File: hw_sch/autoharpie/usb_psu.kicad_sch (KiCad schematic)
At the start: 3 parts, among them J1 USB_C_Receptacle_USB2.0

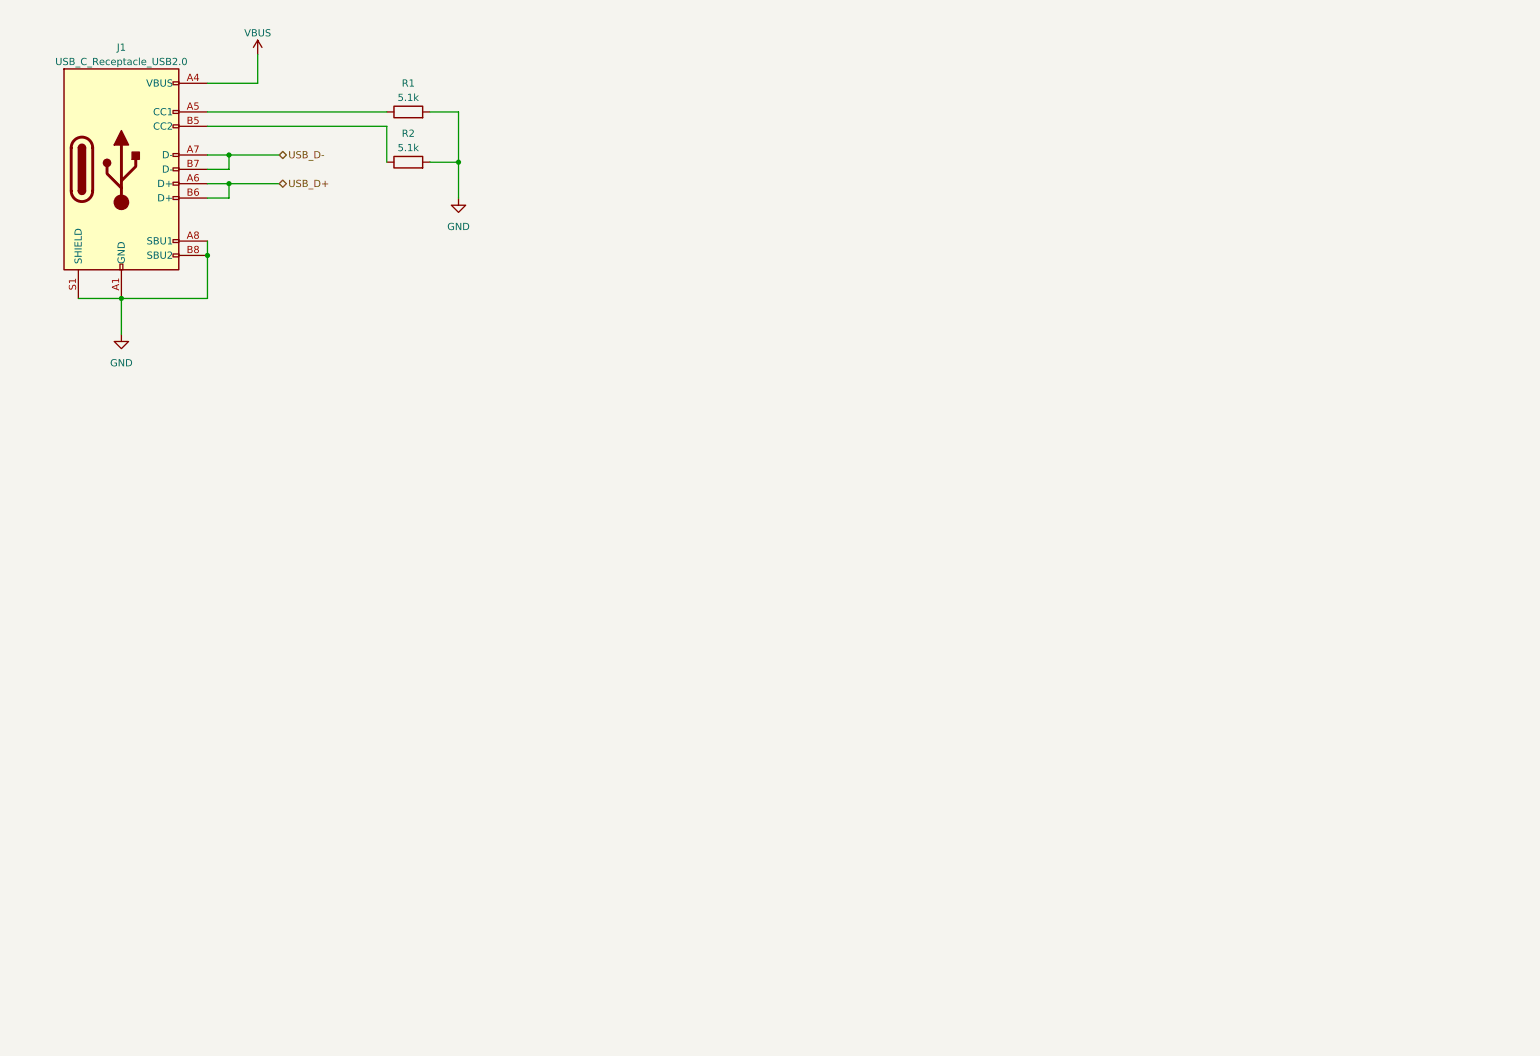
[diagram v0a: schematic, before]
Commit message: teensy mcu chip (imxrt), PSU subsystem work start
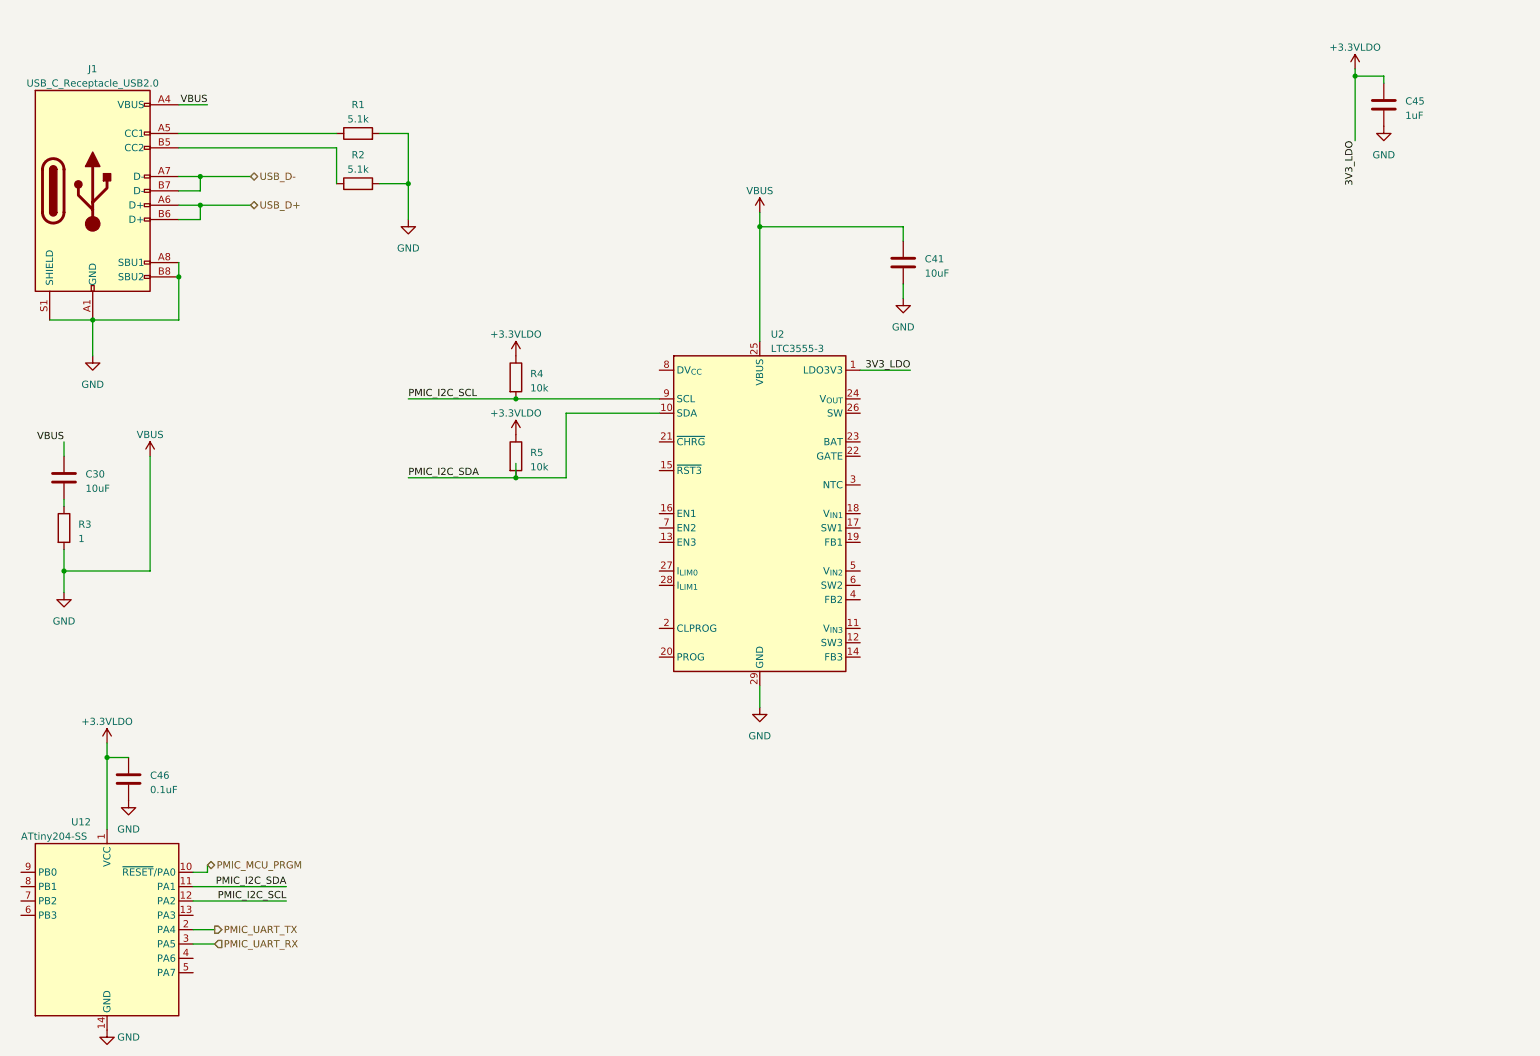
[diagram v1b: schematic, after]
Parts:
- added C30, C41: 10uF, symbol Device:C
- added C45: 1uF, symbol Device:C
- added C46: 0.1uF, symbol Device:C
- added R3: 1, symbol Device:R
- added R4, R5: 10k, symbol Device:R
- added U12: ATtiny204-SS, Package_SO:SOIC-8_3.9x4.9mm_P1.27mm, symbol MCU_Microchip_ATtiny:ATtiny204-SS
- added U2: LTC3555-3, Package_DFN_QFN:QFN-28-1EP_4x5mm_P0.5mm_EP2.65x3.65mm, symbol Battery_Management:LTC3555-3
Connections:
- net VBUS is gone; now on net GND: J1.A4 (VBUS), J1.A9 (VBUS), J1.B4 (VBUS), J1.B9 (VBUS)
- net GND: now also C30.1, C41.1, C41.2, C45.2, C46.2, R3.2, U12.14 (GND), U2.25 (VBUS), U2.29 (GND)
- new net: C30.2, R3.1
- new net +3.3V: C45.1, C46.1, R4.1, R5.1, U12.1 (VCC), U2.1 (LDO3V3)
- new net PMIC_I2C_SCL: R4.2, U12.12 (PA2), U2.9 (SCL)
- new net PMIC_I2C_SDA: R5.2, U12.11 (PA1), U2.10 (SDA)
- new net PMIC_MCU_PRGM: U12.10 (~{RESET}/PA0)
- new net PMIC_UART_RX: U12.3 (PA5)
- new net PMIC_UART_TX: U12.2 (PA4)
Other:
- moved on the sheet: J1, R1, R2

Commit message: switch to teensy reduce pins
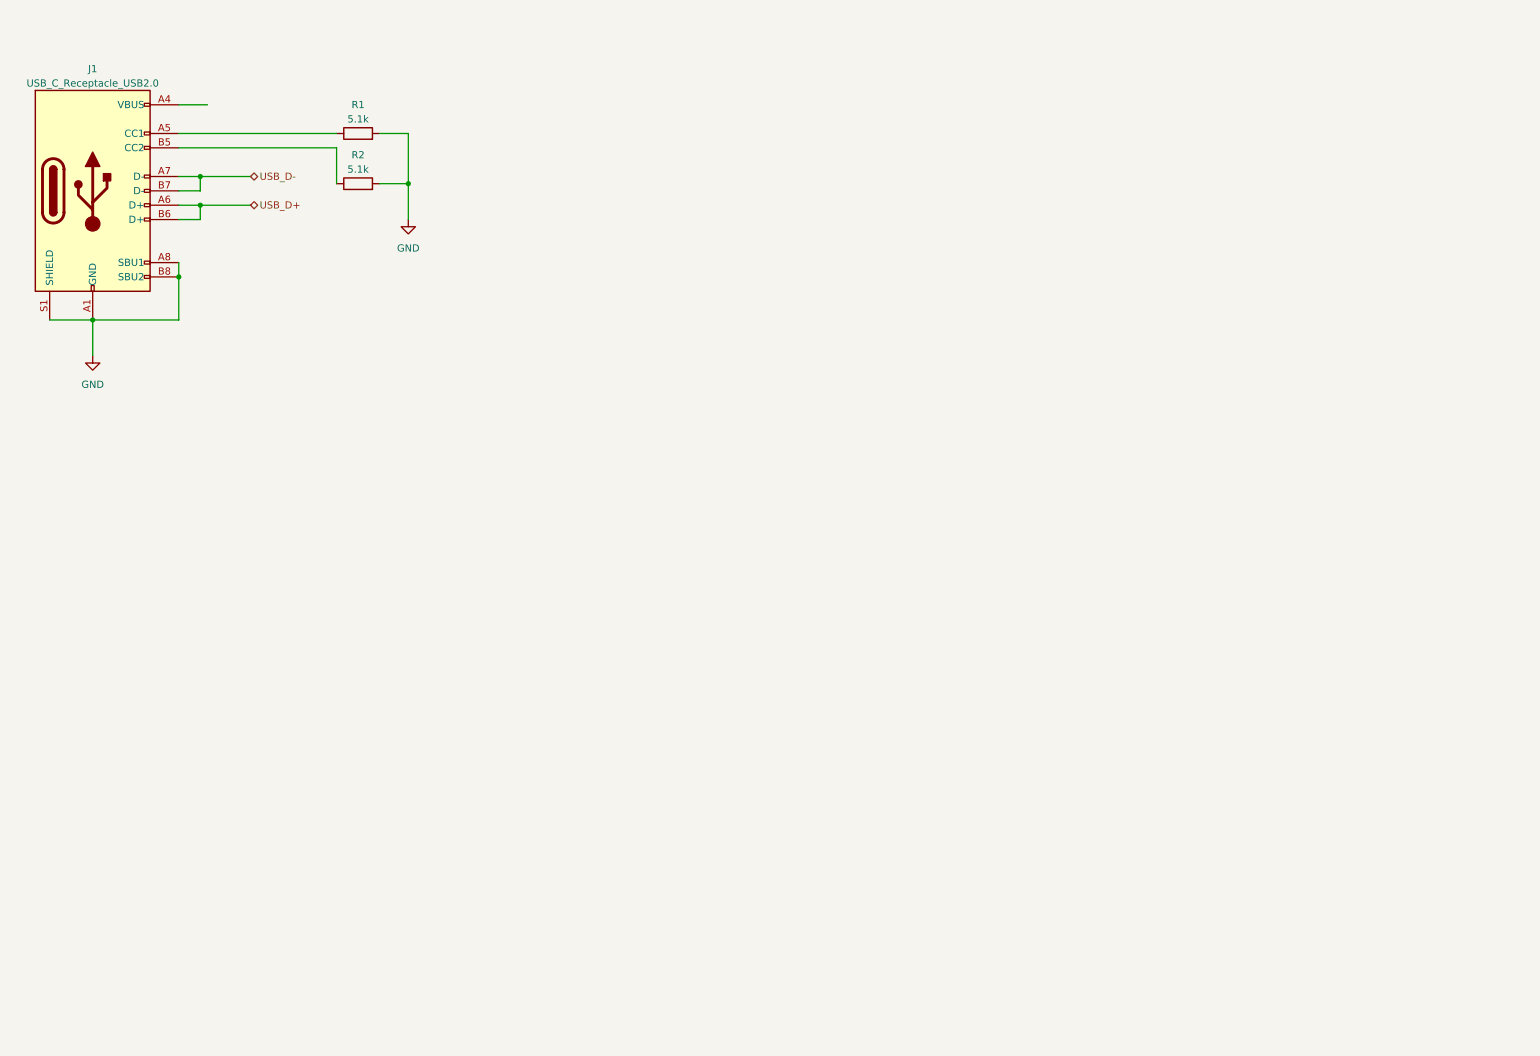
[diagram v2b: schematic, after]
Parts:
- removed C30, C41: 10uF, symbol Device:C
- removed C45: 1uF, symbol Device:C
- removed C46: 0.1uF, symbol Device:C
- removed R3: 1, symbol Device:R
- removed R4, R5: 10k, symbol Device:R
- removed U12: ATtiny204-SS, Package_SO:SOIC-8_3.9x4.9mm_P1.27mm, symbol MCU_Microchip_ATtiny:ATtiny204-SS
- removed U2: LTC3555-3, Package_DFN_QFN:QFN-28-1EP_4x5mm_P0.5mm_EP2.65x3.65mm, symbol Battery_Management:LTC3555-3
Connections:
- net GND: no longer J1.A4 (VBUS), J1.A9 (VBUS), J1.B4 (VBUS), J1.B9 (VBUS)
- new net: J1.A4 (VBUS), J1.A9 (VBUS), J1.B4 (VBUS), J1.B9 (VBUS)

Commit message: matrix, flattening
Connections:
- net VBUS: now reaches J1.A4 (VBUS), J1.A9 (VBUS), J1.B4 (VBUS), J1.B9 (VBUS)
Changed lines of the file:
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@@
   (junction (at 86.36 44.45) (diameter 0) (color 0 0 0 0)
   )
+  (wire (pts (xy 49.53 27.94) (xy 49.53 30.48))
+    (stroke (width 0) (type default))
+  )
   (wire (pts (xy 86.36 35.56) (xy 86.36 44.45))
     (stroke (width 0) (type default))
@@
     (stroke (width 0) (type default))
   )
-  (wire (pts (xy 45.72 30.48) (xy 50.8 30.48))
+  (wire (pts (xy 45.72 30.48) (xy 49.53 30.48))
     (stroke (width 0) (type default))
   )
@@
         )
       )
+    )
+  )
+  (symbol (lib_id "power:VBUS") (at 49.53 27.94 0) (unit 1)
+    (in_bom yes) (on_board yes) (dnp no) (fields_autoplaced)
+    (property "Reference" "#PWR012" (at 49.53 31.75 0)
+      (effects (font (size 1.27 1.27)) hide)
+    )
+    (property "Value" "VBUS" (at 49.53 24.13 0)
+      (effects (font (size 1.27 1.27)))
+    )
+    (property "Footprint" "" (at 49.53 27.94 0)
+      (effects (font (size 1.27 1.27)) hide)
+    )
+    (property "Datasheet" "" (at 49.53 27.94 0)
+      (effects (font (size 1.27 1.27)) hide)
+    )
+    (pin "1")
+    (instances
+      (project "autoharpie"
+        (path "/f22a88c4-866b-40a0-9fc2-96344be0ec71/99b052d6-7969-4dd2-91c7-8bd18b784c30"
+          (reference "#PWR012") (unit 1)
+        )
+      )

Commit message: isolated ground
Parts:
- added C43: 10u, symbol Device:C
- added C44, C45: 330p, symbol Device:C
- added L1: 22u, symbol Device:L
- added U4: RFM-0505S, RFM_RCP, symbol 2023-03-08_01-27-09:RFM-0505S
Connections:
- net GND: now also C43.2, C45.1, U4.2 (+VIN)
- net VBUS: now also C43.1, L1.1
- new net: C44.1, L1.2, U4.1 (-VIN)
- new net 5V_ISO: C44.2, U4.4 (+VOUT)
- new net GND_ISO: C45.2, U4.3 (-VOUT)

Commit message: stm32, msp430
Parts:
- added C51: 10u, symbol Device:C
- added C52, C53: 330p, symbol Device:C
- added C54, C55: 47u, symbol Device:C
- added C70: 0.1u, symbol Device:C
- added D2: PMEG2010AEH, Diode_SMD:D_SOD-123F, symbol Diode:PMEG2010AEH
- added L2: 22u, symbol Device:L
- added L3: 2u2, symbol Device:L
- added R19, R22: 100k, symbol Device:R
- added R29: 33, symbol Device:R
- added U6: RFM-0505S, RFM_RCP, symbol 2023-03-08_01-27-09:RFM-0505S
- added U7: RT6150B-33GQW, 10-WFDFN-EP_RIT, symbol 2023-03-08_23-59-12:RT6150B-33GQW
- added U9: TCMT1100, Package_SO:SOP-4_4.4x2.6mm_P1.27mm, symbol Isolator:TCMT1100
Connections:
- net GND: now also C51.2, C53.1, C54.2, C55.2, C70.2, R22.2, U6.2 (+VIN), U7.11 (GND), U7.3 (GND), U7.9 (GND)
- net VBUS: now also C51.1, D2.2 (A), L2.1
- net 5V_ISO renamed 5V_ISO_CAP
- net GND_ISO renamed GND_ISO_CAP
- net GND_ISO_CAP: now also U9.3
- new net: C52.1, L2.2, U6.1 (-VIN)
- new net: C54.1, D2.1 (K), R19.2, U7.5 (VIN), U7.8 (VINA)
- new net: L3.1, U7.2 (LX2)
- new net: L3.2, U7.4 (LX1)
- new net: R19.1, U7.6 (EN)
- new net: R29.2, U9.1
- new net +3V3: C55.1, C70.1, R29.1, U7.1 (VOUT), U7.10 (FB)
- new net 5V_ISO_AUDIO: C52.2, U6.4 (+VOUT)
- new net CAP_LDO_EN: U9.4
- new net CAP_PWR_ENABLE: U9.2
- new net GND_ISO_AUDIO: C53.2, U6.3 (-VOUT)
- new net PSU_MODE: R22.1, U7.7 (PS)

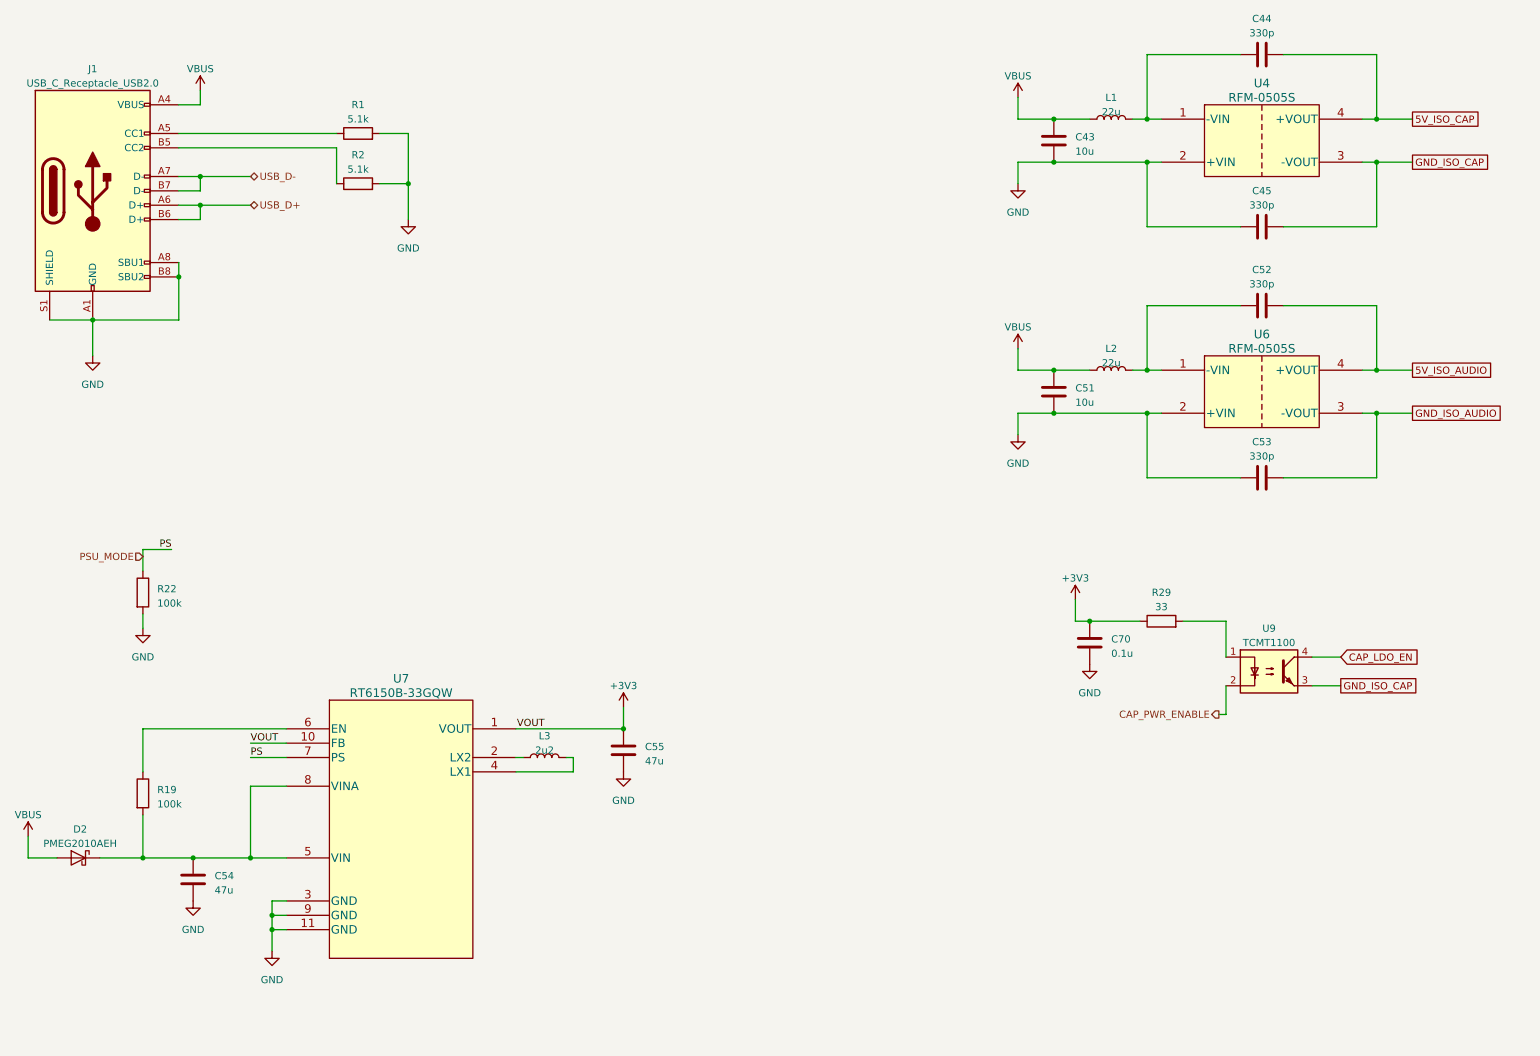
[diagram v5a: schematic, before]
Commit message: DAC wiring, add heirch pins
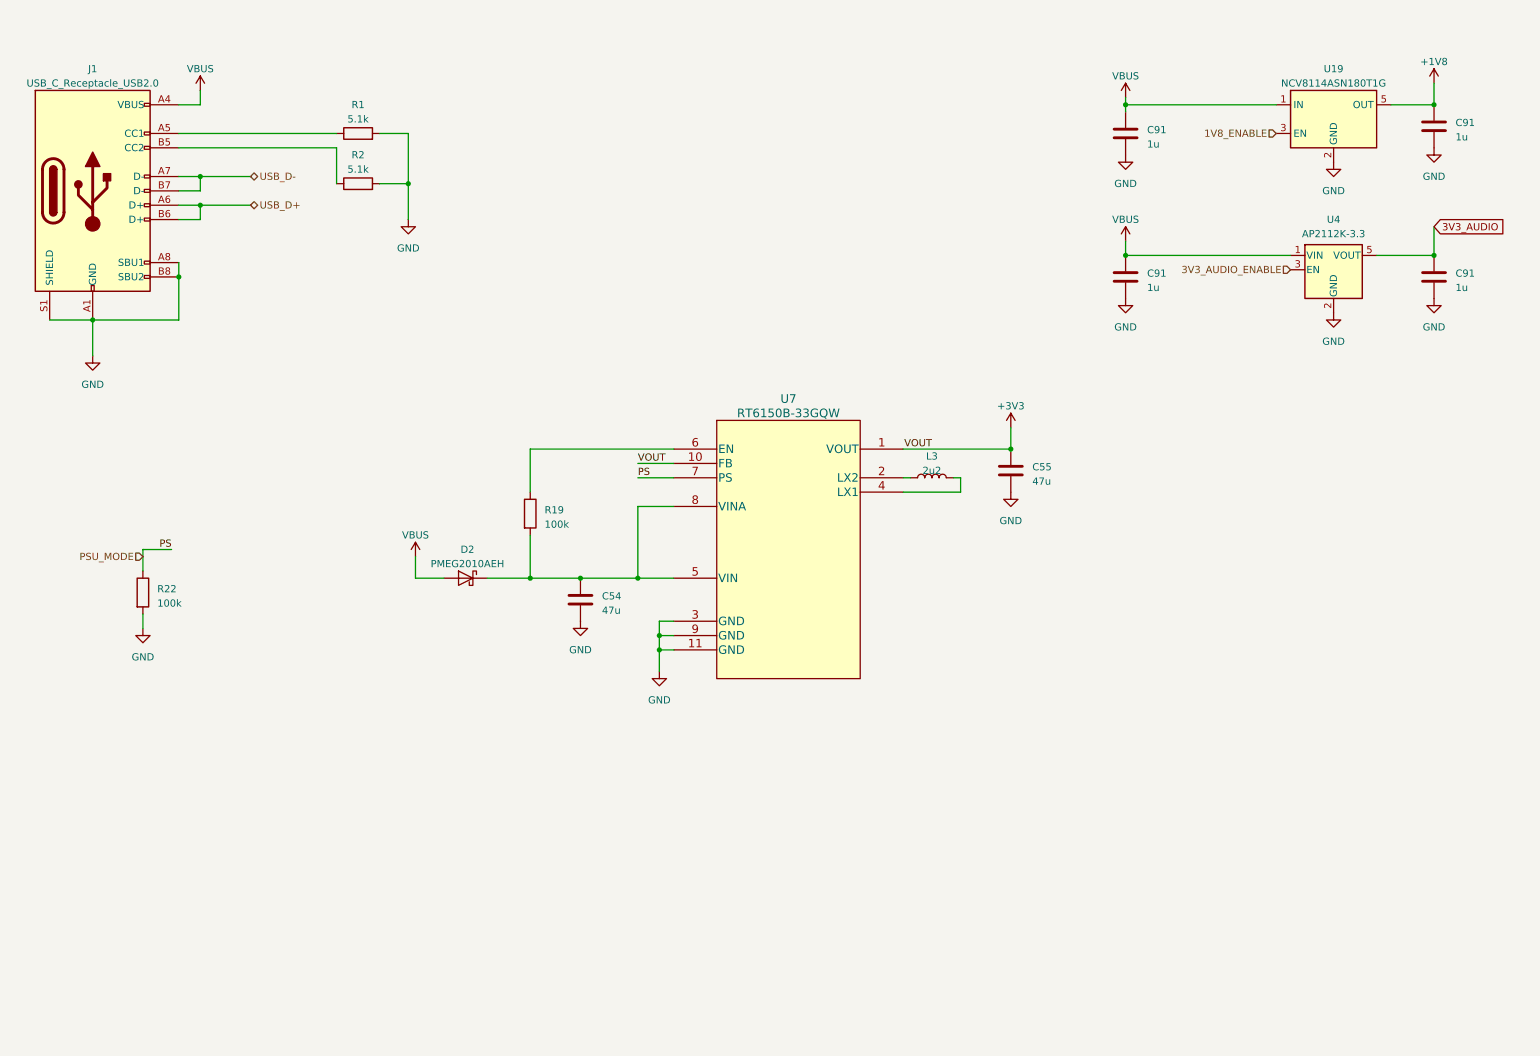
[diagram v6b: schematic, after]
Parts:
- removed C43, C51: 10u, symbol Device:C
- removed C44, C45, C52, C53: 330p, symbol Device:C
- removed C70: 0.1u, symbol Device:C
- removed L1, L2: 22u, symbol Device:L
- removed R29: 33, symbol Device:R
- removed U4, U6: RFM-0505S, RFM_RCP, symbol 2023-03-08_01-27-09:RFM-0505S
- removed U9: TCMT1100, Package_SO:SOP-4_4.4x2.6mm_P1.27mm, symbol Isolator:TCMT1100
- added C91 (x4): 1u, symbol Device:C
- added U19: NCV8114ASN180T1G, Package_TO_SOT_SMD:TSOT-23-5, symbol Regulator_Linear:NCV8114ASN180T1G
- added U4: AP2112K-3.3, Package_TO_SOT_SMD:SOT-23-5, symbol Regulator_Linear:AP2112K-3.3
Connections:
- net GND: now also C91.2, C91.2, C91.2, C91.2, U19.2 (GND), U4.2 (GND)
- net VBUS: now also C91.1, C91.1, U19.1 (IN), U4.1 (VIN)
- new net +1V8: C91.1, U19.5 (OUT)
- new net 1V8_ENABLE: U19.3 (EN)
- new net 3V3_AUDIO: C91.1, U4.5 (VOUT)
- new net 3V3_AUDIO_ENABLE: U4.3 (EN)
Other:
- moved on the sheet: C54, C55, D2, L3, R19, U7
